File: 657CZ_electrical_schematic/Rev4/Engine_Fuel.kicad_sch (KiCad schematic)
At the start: 20 parts, among them SW10 Nose Gear, SW12 AP SERVOS, SW6 Heater, SW7 Fuel Boost, SW8 Canopy, SW9 Lnd Brake

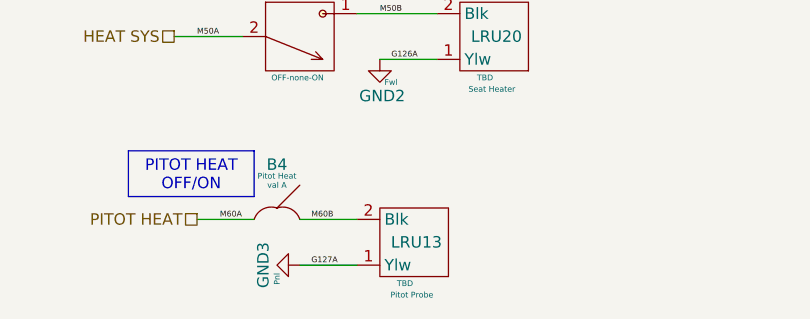
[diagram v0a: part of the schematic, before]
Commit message: added Locations for outstanding components
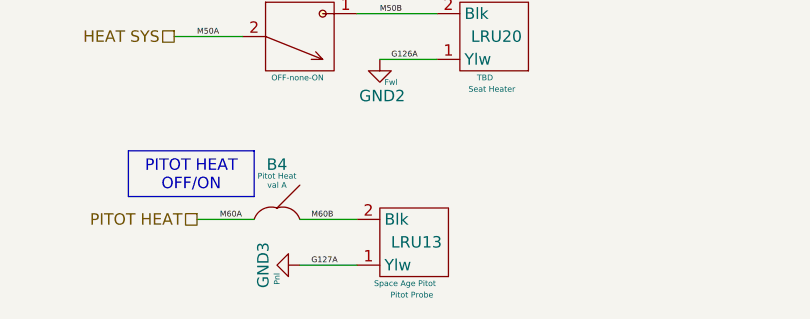
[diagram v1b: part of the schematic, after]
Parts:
- B4: LocLoad (0,0,0)R9.9 -> (41.3,22.9,-3.5)R9.9
- B6: LocLoad (0,0,0)R3 -> (41.3,23.9,-7.2)R3
- B7: LocLoad (0,0,0)R3 -> (41.3,24.9,-7.2)R3
- LRU12: LocLoad (0,0,0)L9.9 -> (122,10,4)L9.9
- LRU13: LocLoad (0,0,0)L9.9 -> (3.9,11.3,2.3)L9.9
- LRU14: LocLoad (0,0,0)L9.9 -> (88.7,23.,-1.5)L9.9
- LRU15: LocLoad (0,0,0)L9.9 -> (81.6,14.7,-1.5)L9.9
- LRU16: LocLoad (0,0,0)L9.9 -> (30.6,14.5,.8)L9.9
- LRU17: LocLoad (0,0,0)L10. -> (122.2,9.6,2.)L10.
- LRU18: LocLoad (0,0,0)L2.8 -> (34.8,8.,-18.7)L2.8
- LRU19: LocLoad (0,0,0)L2.8 -> (162.2,13.8,59.5)L2.8
- LRU20: LocLoad (0,0,0)L9.9 -> (75,9,-1)L9.9
- LRU23: LocLoad (0,0,0)L1.0 -> (33.9,21.8,8.4)L1.0
- LRU4: LocLoad (0,0,0)R20 -> (40,10,-1)R20
- SW10: LocLoad (0,0,0)R20 -> (41.3,10.3,-1.7)R20
- SW12: LocLoad (0,0,0)R20 -> (41.3,12.3,.3)R20
- SW6: LocLoad (0,0,0)R20 -> (41,20,-17)R20
- SW7: LocLoad (0,0,0)R20 -> (41.3,24.9,-2.4)R20
- SW8: LocLoad (0,0,0)R20 -> (41.3,19.6,15.7)R20
- SW9: LocLoad (0,0,0)R20 -> (041.3,10.3,-.7)R20
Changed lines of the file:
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@@
 			)
 		)
-		(property "Datasheet" "TBD"
+		(property "Datasheet" "Space Age Pitot"
 			(at 62.484 169.672 0)
 			(do_not_autoplace yes)
@@
 			)
 		)
-		(property "LocLoad" "(0,0,0)L9.9"
+		(property "LocLoad" "(3.9,11.3,2.3)L9.9"
 			(at 62.23 165.1 0)
 			(effects
@@
 			)
 		)
-		(property "LocLoad" "(0,0,0)L9.9"
+		(property "LocLoad" "(30.6,14.5,.8)L9.9"
 			(at 68.58 115.57 0)
 			(effects
@@
 			)
 		)
-		(property "LocLoad" "(0,0,0)R20"
+		(property "LocLoad" "(41.3,24.9,-2.4)R20"
 			(at 48.26 34.29 0)
 			(effects
@@
 			)
 		)
-		(property "LocLoad" "(0,0,0)L9.9"
+		(property "LocLoad" "(122,10,4)L9.9"
 			(at 63.5 40.64 0)
 			(effects
@@
 			)
 		)
-		(property "LocLoad" "(0,0,0)L9.9"
+		(property "LocLoad" "(75,9,-1)L9.9"
 			(at 71.12 142.24 0)
 			(effects
@@
 			)
 		)
-		(property "LocLoad" "(0,0,0)R9.9"
+		(property "LocLoad" "(41.3,22.9,-3.5)R9.9"
 			(at 48.26 162.56 0)
 			(effects
@@
 			)
 		)
-		(property "LocLoad" "(0,0,0)R20"
+		(property "LocLoad" "(41.3,12.3,.3)R20"
 			(at 129.54 29.21 0)
 			(effects
@@
 			)
 		)
-		(property "LocLoad" "(0,0,0)L9.9"
+		(property "LocLoad" "(81.6,14.7,-1.5)L9.9"
 			(at 87.63 91.44 0)
 			(effects
@@
 			)
 		)
-		(property "LocLoad" "(0,0,0)R20"
+		(property "LocLoad" "(40,10,-1)R20"
 			(at 69.85 83.82 0)
 			(effects
@@
 			)
 		)
-		(property "LocLoad" "(0,0,0)R3"
+		(property "LocLoad" "(41.3,23.9,-7.2)R3"
 			(at 144.78 27.94 0)
 			(effects
@@
 			)
 		)
-		(property "LocLoad" "(0,0,0)R3"
+		(property "LocLoad" "(41.3,24.9,-7.2)R3"
 			(at 144.78 43.18 0)
 			(effects
@@
 			)
 		)
-		(property "LocLoad" "(0,0,0)L2.8"
+		(property "LocLoad" "(34.8,8.,-18.7)L2.8"
 			(at 163.83 45.72 0)
 			(effects
@@
 			)
 		)
-		(property "LocLoad" "(0,0,0)L10."
+		(property "LocLoad" "(122.2,9.6,2.)L10."
 			(at 78.74 33.02 0)
 			(effects
@@
 			)
 		)
-		(property "LocLoad" "(0,0,0)R20"
+		(property "LocLoad" "(41,20,-17)R20"
 			(at 50.8 142.24 0)
 			(effects
@@
 			)
 		)
-		(property "LocLoad" "(0,0,0)L9.9"
+		(property "LocLoad" "(88.7,23.,-1.5)L9.9"
 			(at 68.58 66.04 0)
 			(effects
@@
 			)
 		)
-		(property "LocLoad" "(0,0,0)R20"
+		(property "LocLoad" "(41.3,19.6,15.7)R20"
 			(at 50.8 66.04 0)
 			(effects
@@
 			)
 		)
-		(property "LocLoad" "(0,0,0)R20"
+		(property "LocLoad" "(41.3,10.3,-1.7)R20"
 			(at 50.8 115.57 0)
 			(effects
@@
 			)
 		)
-		(property "LocLoad" "(0,0,0)L2.8"
+		(property "LocLoad" "(162.2,13.8,59.5)L2.8"
 			(at 163.83 30.48 0)
 			(effects
@@
 			)
 		)
-		(property "LocLoad" "(0,0,0)R20"
+		(property "LocLoad" "(041.3,10.3,-.7)R20"
 			(at 50.8 91.44 0)
 			(effects
@@
 			)
 		)
-		(property "LocLoad" "(0,0,0)L1.0"
+		(property "LocLoad" "(33.9,21.8,8.4)L1.0"
 			(at 138.43 63.5 0)
 			(effects
